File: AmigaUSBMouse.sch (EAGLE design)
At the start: 10 parts, among them IC1_4066 4066N, IC2_4066 4066N

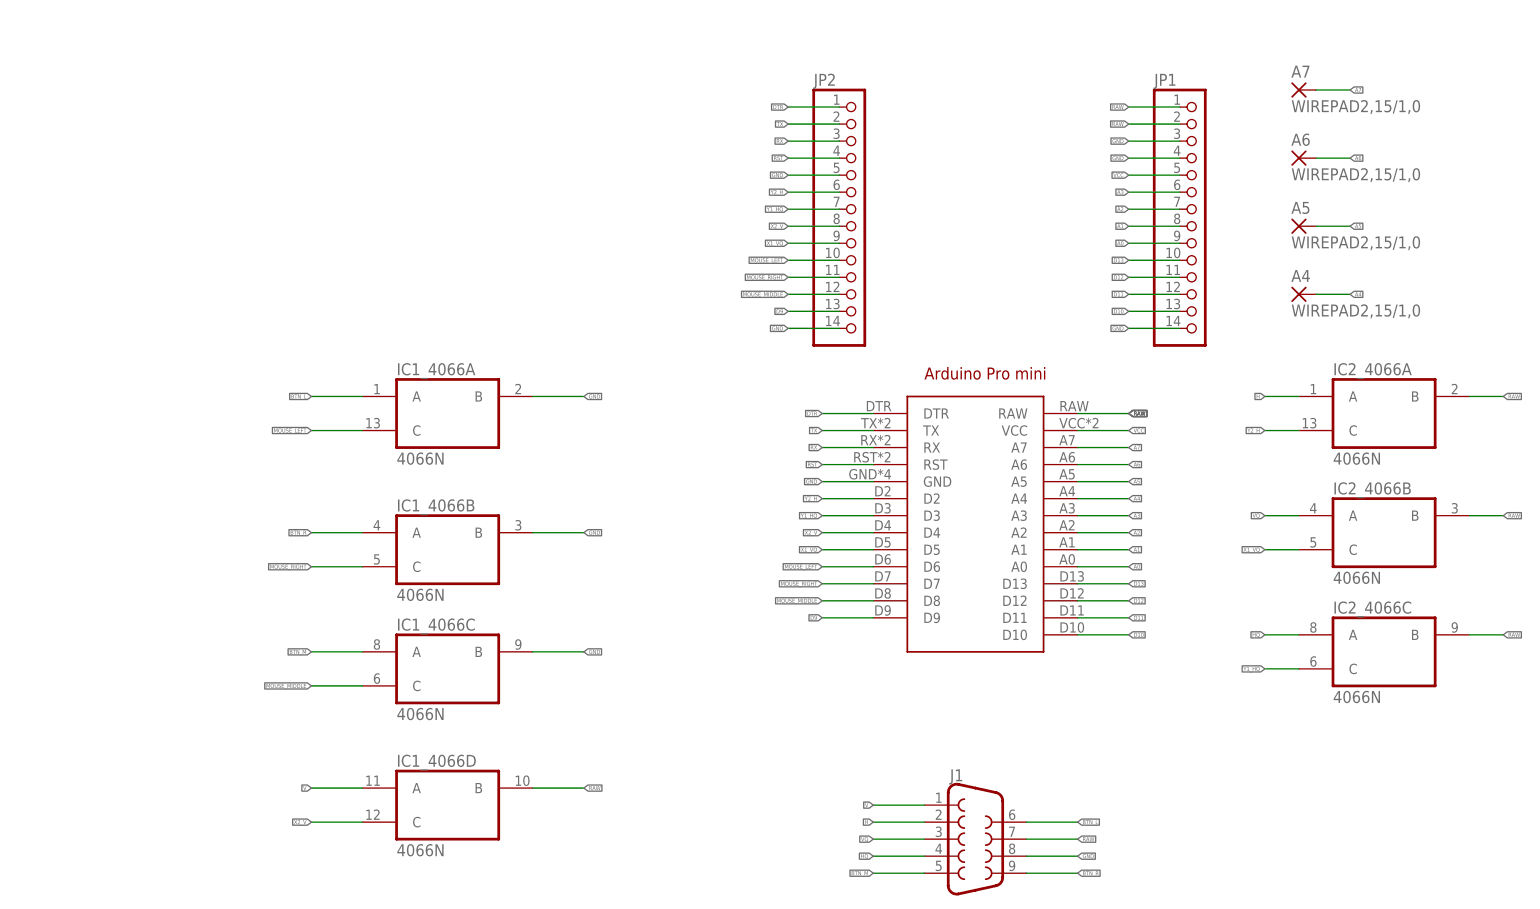
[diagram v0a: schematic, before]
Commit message: Replaced with MOSFETs
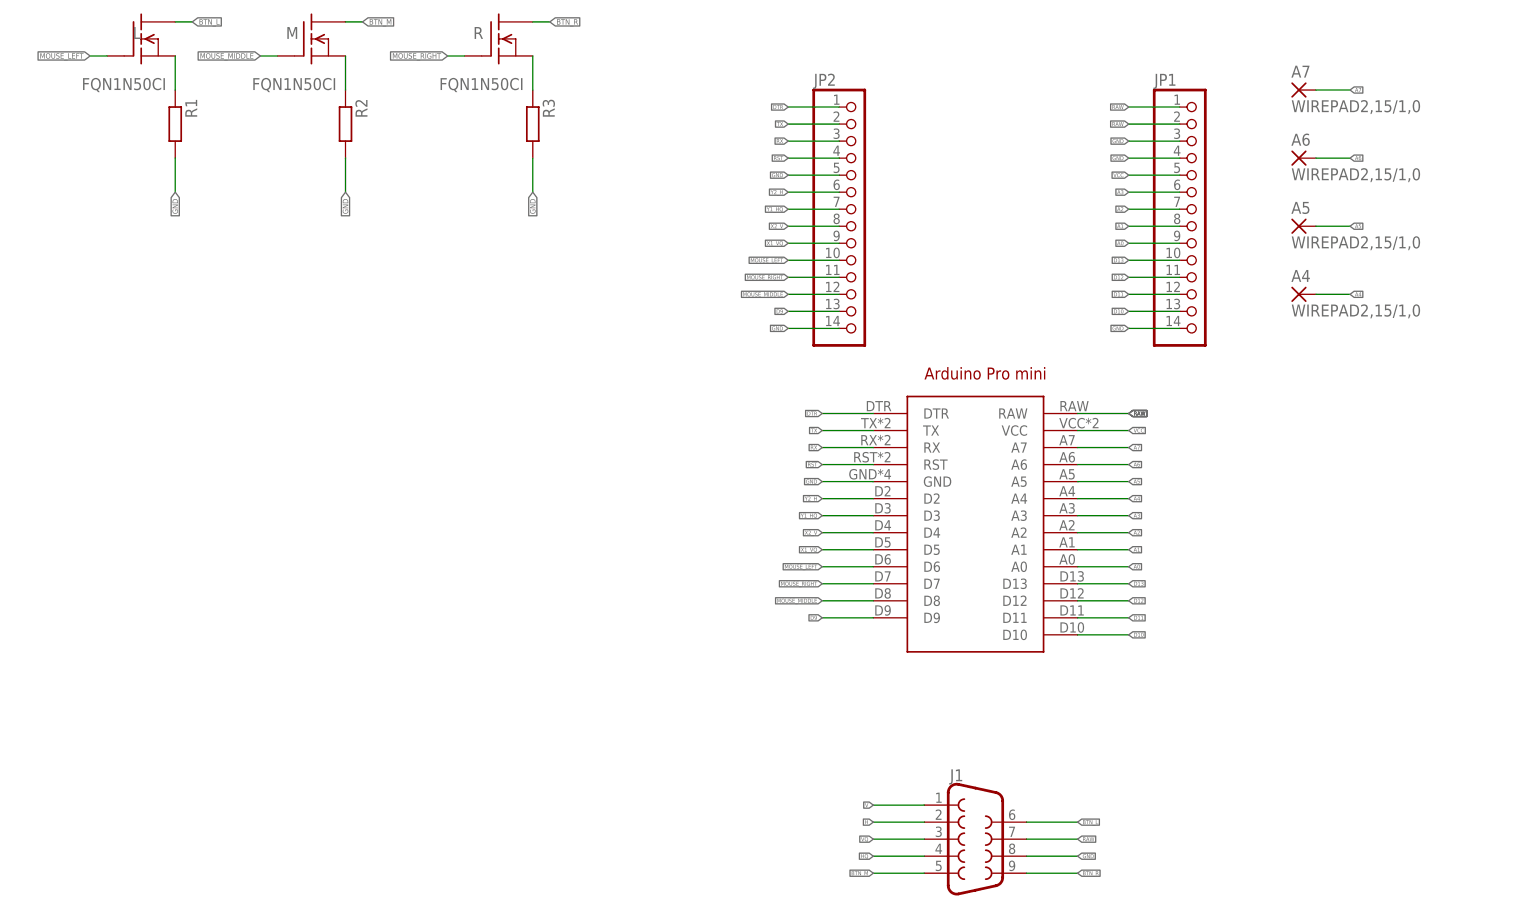
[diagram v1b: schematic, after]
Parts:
- removed IC1_4066, IC2_4066: 4066N, 40xx:4066N
- added L, M, R: FQN1N50CI, adafruit:FQN1N50CI
- added R1, R2, R3: (no value), rcl:R-EU_0204/7
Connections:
- new net N$1: L.S, R1.1
- new net N$2: M.S, R2.1
- new net N$3: R.S, R3.1
- net BTN_L: now also L.D; no longer IC1_4066A.A
- net BTN_M: now also M.D; no longer IC1_4066C.A
- net BTN_R: now also R.D; no longer IC1_4066B.A
- net GND: now also R1.2, R2.2, R3.2; no longer IC1_4066A.B, IC1_4066B.B, IC1_4066C.B
- net H: no longer IC2_4066A.A
- net HQ: no longer IC2_4066C.A
- net MOUSE_LEFT: now also L.G; no longer IC1_4066A.C
- net MOUSE_MIDDLE: now also M.G; no longer IC1_4066C.C
- net MOUSE_RIGHT: now also R.G; no longer IC1_4066B.C
- net RAW: no longer IC1_4066D.B, IC2_4066A.B, IC2_4066B.B, IC2_4066C.B
- net V: no longer IC1_4066D.A
- net VQ: no longer IC2_4066B.A
- net X1_VQ: no longer IC2_4066B.C
- net X2_V: no longer IC1_4066D.C
- net Y1_HQ: no longer IC2_4066C.C
- net Y2_H: no longer IC2_4066A.C

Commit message: Initial
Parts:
- removed A4, A5, A6, A7: WIREPAD2,15/1,0, wirepad:1,6/0,9
- removed ARDUINO1: (no value), arduinopromini:ARDUINO_PRO_MINI
- removed J1: (no value), SparkFun-Connectors:DB9FEMALE
- removed JP1, JP2: (no value), pinhead:PINHD-1X14
- removed R1, R2, R3: (no value), rcl:R-EU_0204/7
- added AMIGA: (no value), SparkFun-Connectors:DB9FEMALE
- added PWR: (no value), pinhead:PINHD-1X2
- added U$1: ABK-PRO-MINI, Arduino-clone:ABK-PRO-MINI
- L, M, R: value FQN1N50CI -> BS108
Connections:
- removed net A4: A4.P, ARDUINO1.A4
- removed net A5: A5.P, ARDUINO1.A5
- removed net H: J1.2
- removed net HQ: J1.4
- removed net N$1: L.S, R1.1
- removed net N$2: M.S, R2.1
- removed net N$3: R.S, R3.1
- removed net RX: ARDUINO1.RX, JP2.3
- removed net TX: ARDUINO1.TX, JP2.2
- removed net V: J1.1
- removed net VQ: J1.3
- new net RST1: U$1.RST1
- new net RX1: U$1.RX1
- new net RX2: U$1.RX1-1
- new net TX1: U$1.TX0
- new net TX2: U$1.TX0-1
- net A0: now also U$1.A0; no longer ARDUINO1.A0, JP1.9
- net A1: now also U$1.A1; no longer ARDUINO1.A1, JP1.8
- net A2: now also U$1.A2; no longer ARDUINO1.A2, JP1.7
- net A3: now also U$1.A3; no longer ARDUINO1.A3, JP1.6
- net A6: now also U$1.A6; no longer A6.P, ARDUINO1.A6
- net A7: now also U$1.A7; no longer A7.P, ARDUINO1.A7
- net BTN_L: now also AMIGA.6; no longer J1.6
- net BTN_M: now also AMIGA.5; no longer J1.5
- net BTN_R: now also AMIGA.9; no longer J1.9
- net D10: now also U$1.D10; no longer ARDUINO1.D10, JP1.13
- net D11: now also U$1.D11; no longer ARDUINO1.D11, JP1.12
- net D12: now also U$1.D12; no longer ARDUINO1.D12, JP1.11
- net D13: now also U$1.D13; no longer ARDUINO1.D13, JP1.10
- net D9: now also U$1.D9; no longer ARDUINO1.D9, JP2.13
- net DTR: now also U$1.DTR; no longer ARDUINO1.DTR, JP2.1
- net GND: now also AMIGA.8, L.S, M.S, PWR.1, R.S, U$1.GND, U$1.GND1, U$1.GND2, U$1.GND3, U$1.GND4; no longer ARDUINO1.GND, J1.8, JP1.14, JP1.3, JP1.4, JP2.14, JP2.5, R1.2, R2.2, R3.2
- net MOUSE_LEFT: now also U$1.D6; no longer ARDUINO1.D6, JP2.10
- net MOUSE_MIDDLE: now also U$1.D8; no longer ARDUINO1.D8, JP2.12
- net MOUSE_RIGHT: now also U$1.D7; no longer ARDUINO1.D7, JP2.11
- net RAW: now also PWR.2, U$1.RAW, U$1.VCC1; no longer ARDUINO1.RAW, J1.7, JP1.1, JP1.2
- net RST: now also U$1.RST; no longer ARDUINO1.RST, JP2.4
- net VCC: now also U$1.VCC; no longer ARDUINO1.VCC, JP1.5
- net X1_VQ: now also AMIGA.3, U$1.D5; no longer ARDUINO1.D5, JP2.9
- net X2_V: now also AMIGA.1, U$1.D4; no longer ARDUINO1.D4, JP2.8
- net Y1_HQ: now also AMIGA.4, U$1.D3; no longer ARDUINO1.D3, JP2.7
- net Y2_H: now also AMIGA.2, U$1.D2; no longer ARDUINO1.D2, JP2.6
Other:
- moved on the sheet: L, M, R
